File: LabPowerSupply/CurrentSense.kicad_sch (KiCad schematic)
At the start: 7 parts

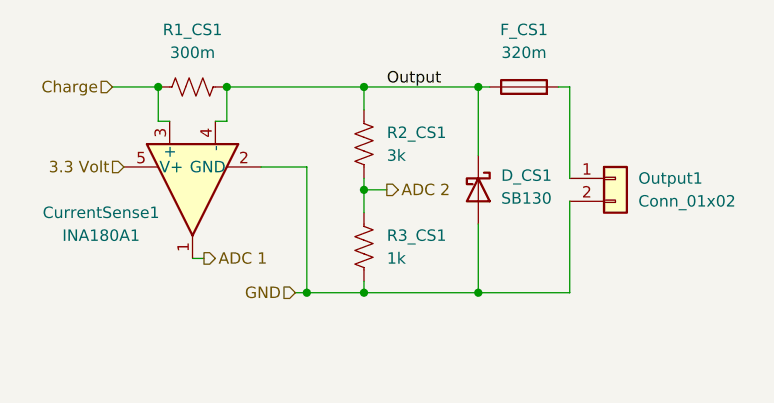
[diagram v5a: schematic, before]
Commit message: Changed most parts to smd
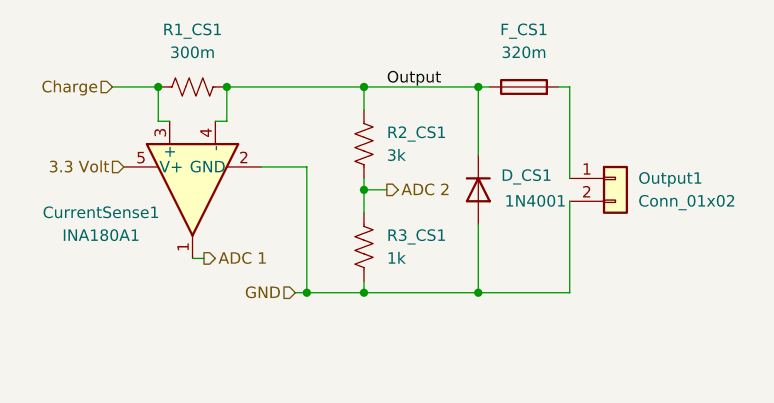
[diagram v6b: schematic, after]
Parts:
- D_CS1: value SB130 -> 1N4001; footprint Diode_THT:D_DO-41_SOD81_P10.16mm_Horizontal -> Diode_SMD:D_SMA; symbol Diode:SB130 -> Diode:1N4001
- F_CS1: footprint Fuse:Fuseholder_Littelfuse_100_series_5x20mm -> Fuse:Fuse_1812_4532Metric
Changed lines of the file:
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@@
     (property "Reference" "F_CS1" (id 0) (at 171.45 77.47 90))
     (property "Value" "320m" (id 1) (at 171.45 80.01 90))
-    (property "Footprint" "Fuse:Fuseholder_Littelfuse_100_series_5x20mm" (id 2) (at 171.45 85.598 90)
+    (property "Footprint" "Fuse:Fuse_1812_4532Metric" (id 2) (at 171.45 85.598 90)
       (effects (font (size 1.27 1.27)) hide)
     )
@@
     (pin "2")
   )
-  (symbol (lib_id "Diode:SB130") (at 166.37 95.25 270) (unit 1)
-    (in_bom yes) (on_board yes) (fields_autoplaced)
+  (symbol (lib_id "Diode:1N4001") (at 166.37 95.25 270) (unit 1)
+    (in_bom yes) (on_board yes)
     (property "Reference" "D_CS1" (id 0) (at 168.91 93.6624 90)
       (effects (font (size 1.27 1.27)) (justify left))
     )
-    (property "Value" "SB130" (id 1) (at 168.91 96.2024 90)
-      (effects (font (size 1.27 1.27)) (justify left))
-    )
-    (property "Footprint" "Diode_THT:D_DO-41_SOD81_P10.16mm_Horizontal" (id 2) (at 161.925 95.25 0)
+    (property "Value" "1N4001" (id 1) (at 172.72 96.52 90))
+    (property "Footprint" "Diode_SMD:D_SMA" (id 2) (at 161.925 95.25 0)
       (effects (font (size 1.27 1.27)) hide)
     )
-    (property "Datasheet" "http://www.diodes.com/_files/datasheets/ds23022.pdf" (id 3) (at 166.37 95.25 0)
+    (property "Datasheet" "http://www.vishay.com/docs/88503/1n4001.pdf" (id 3) (at 166.37 95.25 0)
       (effects (font (size 1.27 1.27)) hide)
     )

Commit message: almost done
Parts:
- added R22_CS2: 1k, Resistor_SMD:R_0603_1608Metric, symbol Device:R_US
- F_CS1: value 320m -> 290m
- R21_CS1: renamed from R2_CS1; value 3k -> 2k
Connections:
- net ADC 2: now also R22_CS2.2; no longer R21_CS1.2
- new net: R21_CS1.2, R22_CS2.1
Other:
- moved on the sheet: D_CS1, Output1, R3_CS1
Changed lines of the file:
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@@
   (junction (at 153.67 83.82) (diameter 0) (color 0 0 0 0)
   )
-  (junction (at 153.67 106.68) (diameter 0) (color 0 0 0 0)
-  )
-  (junction (at 153.67 95.25) (diameter 0) (color 0 0 0 0)
-  )
-  (junction (at 147.32 106.68) (diameter 0) (color 0 0 0 0)
+  (junction (at 153.67 104.14) (diameter 0) (color 0 0 0 0)
+  )
+  (junction (at 153.67 115.57) (diameter 0) (color 0 0 0 0)
+  )
+  (junction (at 147.32 115.57) (diameter 0) (color 0 0 0 0)
   )
   (junction (at 138.43 83.82) (diameter 0) (color 0 0 0 0)
   )
-  (junction (at 166.37 106.68) (diameter 0) (color 0 0 0 0)
+  (junction (at 166.37 115.57) (diameter 0) (color 0 0 0 0)
   )
   (junction (at 166.37 83.82) (diameter 0) (color 0 0 0 0)
@@
     (stroke (width 0) (type default) (color 0 0 0 0))
   )
-  (wire (pts (xy 153.67 106.68) (xy 166.37 106.68))
-    (stroke (width 0) (type default) (color 0 0 0 0))
-  )
-  (wire (pts (xy 147.32 106.68) (xy 153.67 106.68))
+  (wire (pts (xy 153.67 115.57) (xy 166.37 115.57))
+    (stroke (width 0) (type default) (color 0 0 0 0))
+  )
+  (wire (pts (xy 147.32 115.57) (xy 153.67 115.57))
     (stroke (width 0) (type default) (color 0 0 0 0))
   )
@@
     (stroke (width 0) (type default) (color 0 0 0 0))
   )
+  (wire (pts (xy 153.67 101.6) (xy 153.67 104.14))
+    (stroke (width 0) (type default) (color 0 0 0 0))
+  )
   (wire (pts (xy 132.08 87.63) (xy 130.81 87.63))
     (stroke (width 0) (type default) (color 0 0 0 0))
@@
     (stroke (width 0) (type default) (color 0 0 0 0))
   )
-  (wire (pts (xy 166.37 83.82) (xy 166.37 91.44))
+  (wire (pts (xy 166.37 83.82) (xy 166.37 96.52))
     (stroke (width 0) (type default) (color 0 0 0 0))
   )
@@
     (stroke (width 0) (type default) (color 0 0 0 0))
   )
-  (wire (pts (xy 176.53 83.82) (xy 176.53 93.98))
-    (stroke (width 0) (type default) (color 0 0 0 0))
-  )
-  (wire (pts (xy 166.37 106.68) (xy 176.53 106.68))
+  (wire (pts (xy 176.53 83.82) (xy 176.53 100.33))
+    (stroke (width 0) (type default) (color 0 0 0 0))
+  )
+  (wire (pts (xy 166.37 115.57) (xy 176.53 115.57))
+    (stroke (width 0) (type default) (color 0 0 0 0))
+  )
+  (wire (pts (xy 153.67 104.14) (xy 153.67 106.68))
+    (stroke (width 0) (type default) (color 0 0 0 0))
+  )
+  (wire (pts (xy 166.37 104.14) (xy 166.37 115.57))
     (stroke (width 0) (type default) (color 0 0 0 0))
   )
@@
     (stroke (width 0) (type default) (color 0 0 0 0))
   )
-  (wire (pts (xy 153.67 93.98) (xy 153.67 95.25))
-    (stroke (width 0) (type default) (color 0 0 0 0))
-  )
-  (wire (pts (xy 153.67 95.25) (xy 153.67 97.79))
-    (stroke (width 0) (type default) (color 0 0 0 0))
-  )
   (wire (pts (xy 166.37 83.82) (xy 167.64 83.82))
     (stroke (width 0) (type default) (color 0 0 0 0))
   )
-  (wire (pts (xy 147.32 92.71) (xy 147.32 106.68))
-    (stroke (width 0) (type default) (color 0 0 0 0))
-  )
-  (wire (pts (xy 176.53 96.52) (xy 176.53 106.68))
+  (wire (pts (xy 147.32 92.71) (xy 147.32 115.57))
     (stroke (width 0) (type default) (color 0 0 0 0))
   )
@@
     (stroke (width 0) (type default) (color 0 0 0 0))
   )
-  (wire (pts (xy 166.37 99.06) (xy 166.37 106.68))
-    (stroke (width 0) (type default) (color 0 0 0 0))
-  )
-  (wire (pts (xy 153.67 105.41) (xy 153.67 106.68))
-    (stroke (width 0) (type default) (color 0 0 0 0))
-  )
-  (wire (pts (xy 153.67 95.25) (xy 156.21 95.25))
+  (wire (pts (xy 153.67 114.3) (xy 153.67 115.57))
+    (stroke (width 0) (type default) (color 0 0 0 0))
+  )
+  (wire (pts (xy 153.67 104.14) (xy 156.21 104.14))
     (stroke (width 0) (type default) (color 0 0 0 0))
   )
@@
     (stroke (width 0) (type default) (color 0 0 0 0))
   )
-  (wire (pts (xy 146.05 106.68) (xy 147.32 106.68))
+  (wire (pts (xy 176.53 102.87) (xy 176.53 115.57))
+    (stroke (width 0) (type default) (color 0 0 0 0))
+  )
+  (wire (pts (xy 146.05 115.57) (xy 147.32 115.57))
     (stroke (width 0) (type default) (color 0 0 0 0))
   )
@@
     (effects (font (size 1.27 1.27)) (justify right))
   )
-  (hierarchical_label "ADC 2" (shape output) (at 156.21 95.25 0)
+  (hierarchical_label "ADC 2" (shape output) (at 156.21 104.14 0)
     (effects (font (size 1.27 1.27)) (justify left))
   )
-  (hierarchical_label "GND" (shape input) (at 146.05 106.68 180)
+  (hierarchical_label "GND" (shape input) (at 146.05 115.57 180)
     (effects (font (size 1.27 1.27)) (justify right))
   )
@@
     (effects (font (size 1.27 1.27)) (justify right))
   )
+  (symbol (lib_id "Device:R_US") (at 153.67 97.79 0) (unit 1)
+    (in_bom yes) (on_board yes) (fields_autoplaced)
+    (property "Reference" "R22_CS2" (id 0) (at 156.21 96.5199 0)
+      (effects (font (size 1.27 1.27)) (justify left))
+    )
+    (property "Value" "1k" (id 1) (at 156.21 99.0599 0)
+      (effects (font (size 1.27 1.27)) (justify left))
+    )
+    (property "Footprint" "Resistor_SMD:R_0603_1608Metric" (id 2) (at 154.686 98.044 90)
+      (effects (font (size 1.27 1.27)) hide)
+    )
+    (property "Datasheet" "~" (id 3) (at 153.67 97.79 0)
+      (effects (font (size 1.27 1.27)) hide)
+    )
+    (pin "1")
+    (pin "2")
+  )
   (symbol (lib_id "Device:Fuse") (at 171.45 83.82 90) (unit 1)
     (in_bom yes) (on_board yes) (fields_autoplaced)
     (property "Reference" "F_CS1" (id 0) (at 171.45 77.47 90))
-    (property "Value" "320m" (id 1) (at 171.45 80.01 90))
+    (property "Value" "290m" (id 1) (at 171.45 80.01 90))
     (property "Footprint" "Fuse:Fuse_1812_4532Metric" (id 2) (at 171.45 85.598 90)
       (effects (font (size 1.27 1.27)) hide)
@@
   (symbol (lib_id "Device:R_US") (at 153.67 90.17 0) (unit 1)
     (in_bom yes) (on_board yes) (fields_autoplaced)
-    (property "Reference" "R2_CS1" (id 0) (at 156.21 88.8999 0)
-      (effects (font (size 1.27 1.27)) (justify left))
-    )
-    (property "Value" "3k" (id 1) (at 156.21 91.4399 0)
+    (property "Reference" "R21_CS1" (id 0) (at 156.21 88.8999 0)
+      (effects (font (size 1.27 1.27)) (justify left))
+    )
+    (property "Value" "2k" (id 1) (at 156.21 91.4399 0)
       (effects (font (size 1.27 1.27)) (justify left))
     )
@@
     (pin "5")
   )
-  (symbol (lib_id "Connector_Generic:Conn_01x02") (at 181.61 93.98 0) (unit 1)
-    (in_bom yes) (on_board yes) (fields_autoplaced)
-    (property "Reference" "Output1" (id 0) (at 184.15 93.9799 0)
-      (effects (font (size 1.27 1.27)) (justify left))
-    )
-    (property "Value" "Conn_01x02" (id 1) (at 184.15 96.5199 0)
-      (effects (font (size 1.27 1.27)) (justify left))
-    )
-    (property "Footprint" "Connector_Wire:SolderWire-2sqmm_1x02_P7.8mm_D2mm_OD3.9mm" (id 2) (at 181.61 93.98 0)
-      (effects (font (size 1.27 1.27)) hide)
-    )
-    (property "Datasheet" "~" (id 3) (at 181.61 93.98 0)
-      (effects (font (size 1.27 1.27)) hide)
-    )
-    (pin "1")
-    (pin "2")
-  )
-  (symbol (lib_id "Diode:1N4001") (at 166.37 95.25 270) (unit 1)
+  (symbol (lib_id "Connector_Generic:Conn_01x02") (at 181.61 100.33 0) (unit 1)
     (in_bom yes) (on_board yes)
-    (property "Reference" "D_CS1" (id 0) (at 168.91 93.6624 90)
-      (effects (font (size 1.27 1.27)) (justify left))
-    )
-    (property "Value" "1N4001" (id 1) (at 172.72 96.52 90))
-    (property "Footprint" "Diode_SMD:D_SMA" (id 2) (at 161.925 95.25 0)
-      (effects (font (size 1.27 1.27)) hide)
-    )
-    (property "Datasheet" "http://www.vishay.com/docs/88503/1n4001.pdf" (id 3) (at 166.37 95.25 0)
-      (effects (font (size 1.27 1.27)) hide)
-    )
-    (pin "1")
-    (pin "2")
-  )
-  (symbol (lib_id "Device:R_US") (at 153.67 101.6 0) (unit 1)
-    (in_bom yes) (on_board yes) (fields_autoplaced)
-    (property "Reference" "R3_CS1" (id 0) (at 156.21 100.3299 0)
-      (effects (font (size 1.27 1.27)) (justify left))
-    )
-    (property "Value" "1k" (id 1) (at 156.21 102.8699 0)
-      (effects (font (size 1.27 1.27)) (justify left))
-    )
-    (property "Footprint" "Resistor_SMD:R_0603_1608Metric" (id 2) (at 154.686 101.854 90)
-      (effects (font (size 1.27 1.27)) hide)
-    )
-    (property "Datasheet" "~" (id 3) (at 153.67 101.6 0)
-      (effects (font (size 1.27 1.27)) hide)
-    )
+    (property "Reference" "Output1" (id 0) (at 184.15 100.3299 0)
+      (effects (font (size 1.27 1.27)) (justify left))
+    )
+    (property "Value" "Conn_01x02" (id 1) (at 184.15 102.87 0)
+      (effects (font (size 1.27 1.27)) (justify left))
+    )
+    (property "Footprint" "Connector_Wire:SolderWire-2sqmm_1x02_P7.8mm_D2mm_OD3.9mm" (id 2) (at 181.61 100.33 0)
+      (effects (font (size 1.27 1.27)) hide)
+    )
+    (property "Datasheet" "~" (id 3) (at 181.61 100.33 0)
+      (effects (font (size 1.27 1.27)) hide)
+    )
+    (pin "1")
+    (pin "2")
+  )
+  (symbol (lib_id "Diode:1N4001") (at 166.37 100.33 270) (unit 1)
+    (in_bom yes) (on_board yes)
+    (property "Reference" "D_CS1" (id 0) (at 168.91 98.7424 90)
+      (effects (font (size 1.27 1.27)) (justify left))
+    )
+    (property "Value" "1N4001" (id 1) (at 172.72 101.6 90))
+    (property "Footprint" "Diode_SMD:D_SMA" (id 2) (at 161.925 100.33 0)
+      (effects (font (size 1.27 1.27)) hide)
+    )
+    (property "Datasheet" "http://www.vishay.com/docs/88503/1n4001.pdf" (id 3) (at 166.37 100.33 0)
+      (effects (font (size 1.27 1.27)) hide)
+    )
+    (pin "1")
+    (pin "2")
+  )
+  (symbol (lib_id "Device:R_US") (at 153.67 110.49 0) (unit 1)
+    (in_bom yes) (on_board yes) (fields_autoplaced)
+    (property "Reference" "R3_CS1" (id 0) (at 156.21 109.2199 0)
+      (effects (font (size 1.27 1.27)) (justify left))
+    )
+    (property "Value" "1k" (id 1) (at 156.21 111.7599 0)
+      (effects (font (size 1.27 1.27)) (justify left))
+    )
+    (property "Footprint" "Resistor_SMD:R_0603_1608Metric" (id 2) (at 154.686 110.744 90)
+      (effects (font (size 1.27 1.27)) hide)
+    )
+    (property "Datasheet" "~" (id 3) (at 153.67 110.49 0)
+      (effects (font (size 1.27 1.27)) hide)
+    )

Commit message: Update pcb footprints
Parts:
- renumbered R22_CS2 to R22_CS1
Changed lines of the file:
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@@
   (symbol (lib_id "Device:R_US") (at 153.67 97.79 0) (unit 1)
     (in_bom yes) (on_board yes) (fields_autoplaced)
-    (property "Reference" "R22_CS2" (id 0) (at 156.21 96.5199 0)
+    (property "Reference" "R22_CS1" (id 0) (at 156.21 96.5199 0)
       (effects (font (size 1.27 1.27)) (justify left))
     )
